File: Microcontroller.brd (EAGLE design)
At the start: 160 x 100 mm, 134 parts, among them Q1 200mA/40V, Q2 200mA/40V, Q3 200mA/40V, Q4 200mA/40V, U1 LM46000PWPR

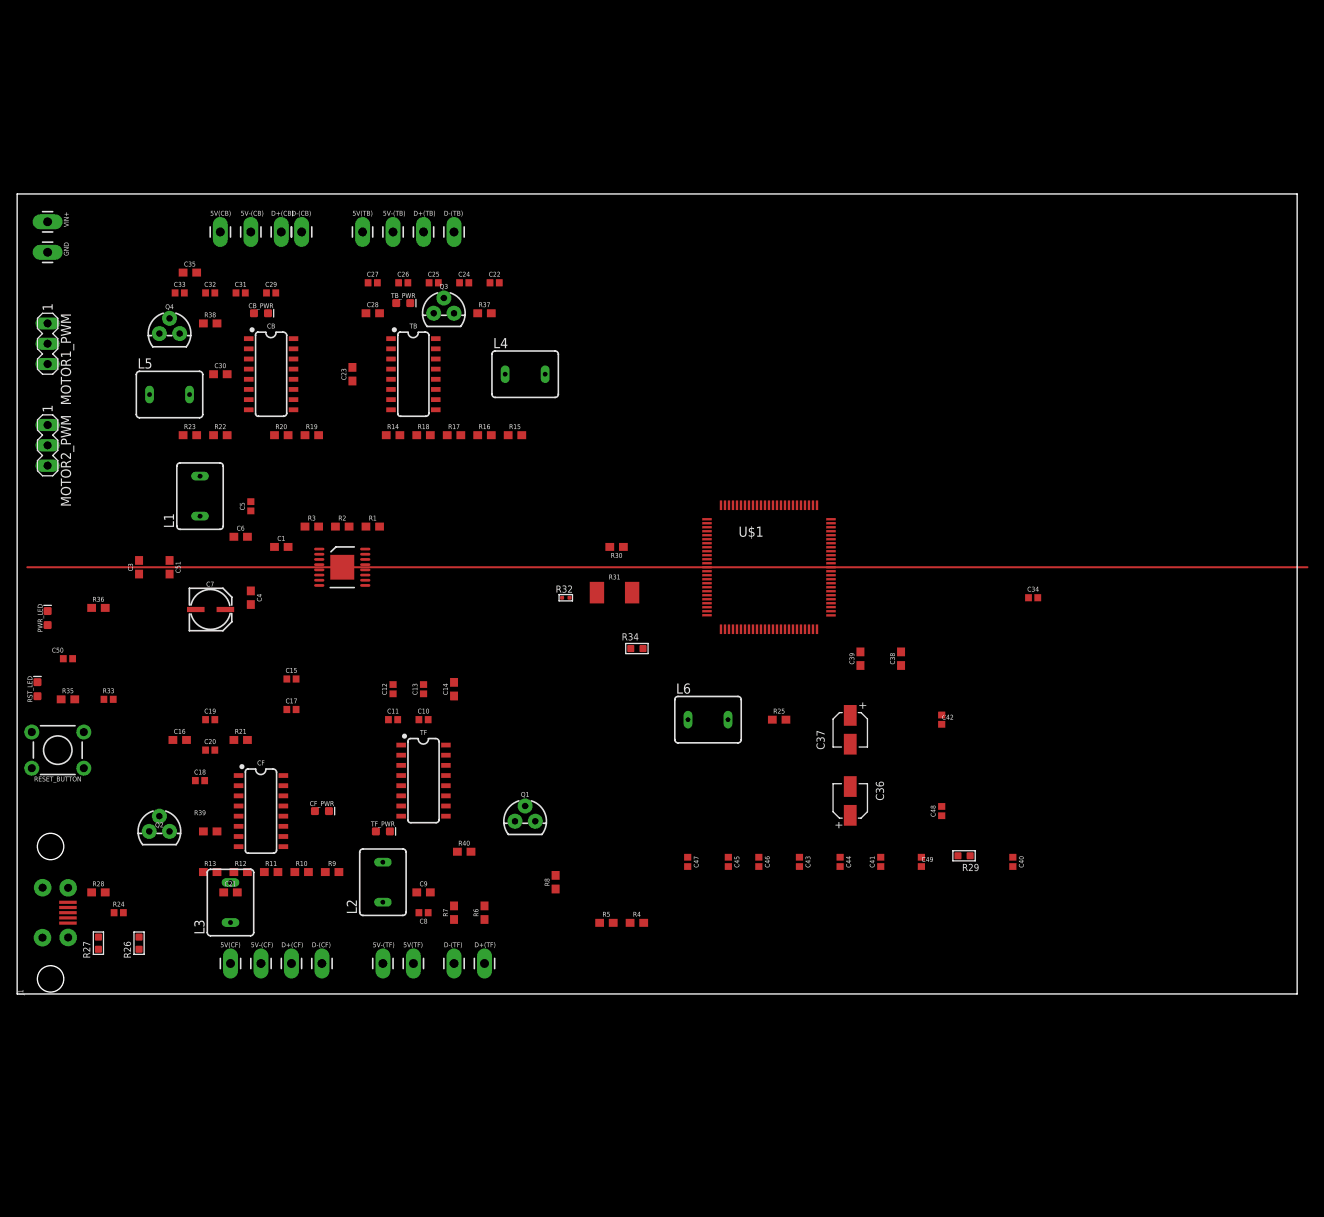
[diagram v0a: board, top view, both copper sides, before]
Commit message: Added strain gauge flex board.
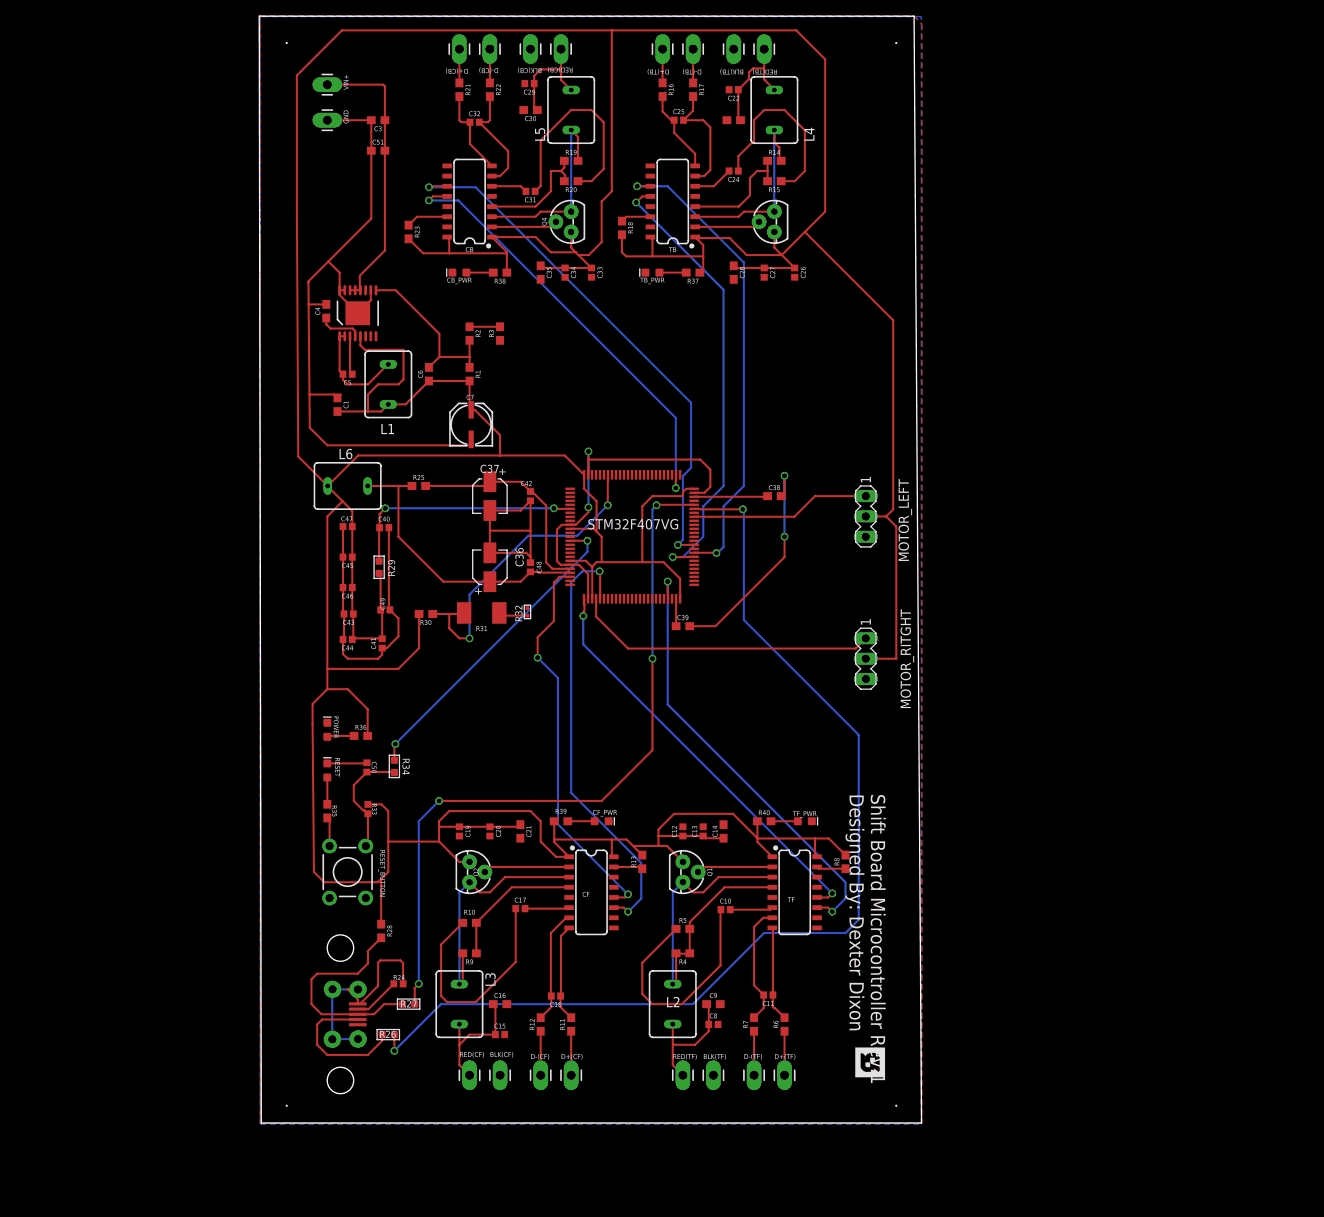
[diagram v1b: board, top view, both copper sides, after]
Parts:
- removed 5V(CB), 5V(CF), 5V(TB), 5V(TF), 5V-(CB), 5V-(CF), 5V-(TB), 5V-(TF): (no value), SparkFun-Connectors:1X01_LONGPAD
- removed MOTOR1_PWM, MOTOR2_PWM: (no value), con-lstb:MA03-1
- removed PWR_LED: BLUE, SparkFun-LED:LED-0603
- removed RST_LED: RED, SparkFun-LED:LED-0603
- removed U$1: STM32F4V_100PIN_GENERIC, stm32f4:LQFP100
- added BLK(CB), BLK(CF), BLK(TB), BLK(TF), RED(CB), RED(CF), RED(TB), RED(TF): (no value), SparkFun-Connectors:1X01_LONGPAD
- added MOTOR_LEFT, MOTOR_RITGHT: (no value), con-lstb:MA03-1
- added POWER: BLUE, SparkFun-LED:LED-0603
- added RESET: RED, SparkFun-LED:LED-0603
- added STM32F407VG: STM32F4V_100PIN_GENERIC, stm32f4:LQFP100
- moved C40 89.0 mm to (45.9, 58.3), turned to 0 degrees
- moved R21 85.8 mm to (55.3, 113.0), turned to 270 degrees
- moved R29 81.5 mm to (45.3, 53.3), turned to 180 degrees
- moved C49 74.0 mm to (46.0, 48.0), turned to 0 degrees
- moved C34 71.2 mm to (68.5, 90.2), turned to 270 degrees
- moved C41 68.0 mm to (45.6, 43.8)
- moved C44 67.5 mm to (41.3, 44.3), turned to 180 degrees
- moved C43 64.3 mm to (41.4, 47.5), turned to 180 degrees
- moved C3 63.4 mm to (45.1, 109.2), turned to 180 degrees
- moved C46 61.8 mm to (41.3, 50.8), turned to 180 degrees
- moved L5 61.5 mm to (69.3, 110.5), turned to 90 degrees
- moved C45 61.0 mm to (41.3, 54.6), turned to 180 degrees
- moved C48 59.8 mm to (64.2, 53.3), turned to 270 degrees
- moved C47 59.7 mm to (41.3, 58.4), turned to 180 degrees
- moved R14 58.7 mm to (94.7, 104.1)
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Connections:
- removed net 3.3V: 5V-(CB).1, 5V-(CF).1, 5V-(TB).1, 5V-(TF).1, C10.1, C12.2, C13.2, C14.2, C15.2, C16.2, C17.1, C19.2, C20.2, C21.2, C22.2, C23.2, C24.1, C26.2, C27.2, C28.2, C29.2, C30.2, C31.1, C33.2, C34.2, C35.2, C36.2, C37.2, C38.2, C39.2, C40.2, C41.1, C42.2, C43.2, C44.2, C45.2, C46.2, C47.2, C48.1, C49.2, C50.2, C8.2, C9.2, CB.14, CB.15, CB_PWR.C, CF.14, CF.15, CF_PWR.C, J1.GND, J1.SHLD1, J1.SHLD2, J1.SHLD3, J1.SHLD4, PWR_LED.C, R10.1, R13.1, R15.1, R18.1, R20.1, R23.1, R24.1, R32.2, R5.1, R8.1, RST_LED.C, TB.14, TB.15, TB_PWR.C, TF.14, TF.15, TF_PWR.C, U$1.PDR_ON, U$1.VSS1, U$1.VSS2, U$1.VSS3, U$1.VSSA
- removed net 3.6V-: C1.1, C3.2, C4.2, C51.1, C7.-, GND.1, R3.1, U1.10, U1.15, U1.16, U1.17, U1.6
- removed net GND: MOTOR1_PWM.3, MOTOR2_PWM.3
- removed net PWM(RIGHT: MOTOR2_PWM.1
- new net 3.3V-: BLK(CB).1, BLK(CF).1, BLK(TB).1, BLK(TF).1, C1.1, C10.1, C12.2, C13.2, C14.2, C15.2, C16.2, C17.1, C19.2, C20.2, C21.2, C22.2, C23.2, C24.1, C26.2, C27.2, C28.2, C29.2, C3.2, C30.2, C31.1, C33.2, C34.2, C35.2, C36.2, C37.2, C38.2, C39.2, C4.2, C40.2, C41.1, C42.2, C43.2, C44.2, C45.2, C46.2, C47.2, C48.1, C49.2, C50.2, C51.1, C7.-, C8.2, C9.2, CB.14, CB.15, CB_PWR.C, CF.14, CF.15, CF_PWR.C, GND.1, J1.GND, J1.SHLD1, J1.SHLD2, J1.SHLD3, J1.SHLD4, MOTOR_LEFT.3, MOTOR_RITGHT.3, POWER.C, R10.1, R13.1, R15.1, R18.1, R20.1, R23.1, R24.1, R3.1, R32.2, R5.1, R8.1, RESET.C, STM32F407VG.PDR_ON, STM32F407VG.VSS1, STM32F407VG.VSS2, STM32F407VG.VSS3, STM32F407VG.VSSA, TB.14, TB.15, TB_PWR.C, TF.14, TF.15, TF_PWR.C, U1.10, U1.15, U1.16, U1.17, U1.6
- net 3.6V+: now also MOTOR_LEFT.2, MOTOR_RITGHT.2, STM32F407VG.VDD1, STM32F407VG.VDD2, STM32F407VG.VDD3, STM32F407VG.VDD4, STM32F407VG.VDD5, STM32F407VG.VDD6; no longer MOTOR1_PWM.2, MOTOR2_PWM.2, U$1.VDD1, U$1.VDD2, U$1.VDD3, U$1.VDD4, U$1.VDD5, U$1.VDD6
- net ANALOG1: now also STM32F407VG.PD15; no longer U$1.PD15
- net DOUT(CB): now also STM32F407VG.PA15; no longer U$1.PA15, U$1.PD13
- net DOUT(CF): now also STM32F407VG.PA0; no longer U$1.PA0
- net DOUT(TB): now also STM32F407VG.PD11; no longer U$1.PD11
- net DOUT(TF): now also STM32F407VG.PA3; no longer U$1.PA3
- net N$17: now also RED(CF).1; no longer 5V(CF).1
- net N$26: now also RED(TB).1; no longer 5V(TB).1
- net N$35: now also RED(CB).1; no longer 5V(CB).1
- net N$43: now also STM32F407VG.VCAP1; no longer U$1.VCAP1
- net N$44: now also STM32F407VG.VCAP2; no longer U$1.VCAP2
- net N$47: now also STM32F407VG.BOOT0; no longer U$1.BOOT0
- net N$5: now also RED(TF).1; no longer 5V(TF).1
- net N$51: now also RESET.A; no longer RST_LED.A
- net N$53: now also STM32F407VG.VREF+; no longer U$1.VREF+
- net N$54: now also POWER.A; no longer PWR_LED.A
- net NRST: now also STM32F407VG.NRST; no longer U$1.NRST
- net PWM(LEFT): now also MOTOR_LEFT.1, STM32F407VG.PA9; no longer MOTOR1_PWM.1, U$1.PA9
- net PWM(RIGHT): now also MOTOR_RITGHT.1, STM32F407VG.PA4; no longer U$1.PA4
- net SCK(CB): now also STM32F407VG.PD14; no longer U$1.PD14
- net SCK(CF): now also STM32F407VG.PA5; no longer U$1.PA5
- net SCK(TB): now also STM32F407VG.PD12; no longer U$1.PD12
- net SCK(TF): now also STM32F407VG.PB10; no longer U$1.PB10
- net SWCLK: now also STM32F407VG.PA14; no longer U$1.PA14
- net SWDIO: now also STM32F407VG.PA13; no longer U$1.PA13
- net USB_DM: now also STM32F407VG.PA11; no longer U$1.PA11
- net USB_DP: now also STM32F407VG.PA12; no longer U$1.PA12
- net VBAT: now also STM32F407VG.VBAT; no longer U$1.VBAT
- net VDDA: now also STM32F407VG.VDDA; no longer U$1.VDDA
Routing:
- net 3.6V+: track 0.00 -> 716.4 mm
- net 3.3V-: track 0.00 -> 387.2 mm, vias 0 -> 4
- net N$59: track 160.0 -> 0.00 mm
- net USB_DM: track 0.00 -> 130.3 mm, vias 0 -> 2
- net USB_DP: track 0.00 -> 91.5 mm, vias 0 -> 4
- net SCK(CB): track 0.00 -> 66.8 mm, vias 0 -> 2
- net SCK(TB): track 0.00 -> 59.5 mm, vias 0 -> 2
- net DOUT(TB): track 0.00 -> 57.0 mm, vias 0 -> 2
- net SCK(TF): track 0.00 -> 55.5 mm, vias 0 -> 2
- net DOUT(CB): track 0.00 -> 55.0 mm, vias 0 -> 2
- net SCK(CF): track 0.00 -> 55.0 mm, vias 0 -> 2
- net DOUT(TF): track 0.00 -> 51.9 mm, vias 0 -> 2
- net DOUT(CF): track 0.00 -> 48.8 mm, vias 0 -> 2
- net N$47: track 0.00 -> 40.0 mm, vias 0 -> 2
- net NRST: track 0.00 -> 39.6 mm, vias 0 -> 2
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- added copper zone on layer 1, net 3.3V-
- added copper zone on layer 16, net 3.3V-
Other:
- board size 160 x 100 mm -> 82.8 x 138.4 mm
- board text added: "Shift Board Microcontroller Rev.1 Designed By: Dexter Dixon"
